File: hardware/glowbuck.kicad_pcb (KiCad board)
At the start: 4 copper layers, 80 x 50 mm, 128 parts, among them J1 Conn_01x04_Socket, J101 Conn_01x01_Pin, J102 Conn_01x01_Pin, J105 Conn_01x01_Pin, J106 Conn_01x01_Pin, J107 Conn_01x01_Pin, J201 USB_C_Receptacle_USB2.0_16P, J202 USB_C_Receptacle_USB2.0_16P, J3 Conn_02x08_Counter_Clockwise, Q401 2N7002NXAKR, SW101 SW_Push, SW102 SW_Push, U101 ESP32-S3-WROOM-1, U102 SN74LVC1T45DBV, U103 INA181A3, U201 TPS25730D, U202 TPD2E2U06DCK, U301 AP63203WU, U401 SIC437A

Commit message: Global labels, explanation texts, fix spring connector
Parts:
- removed J101, J102: Conn_01x01_Pin, TestPoint:TestPoint_Pad_3.0x3.0mm
- added H4: MountingHole, MountingHole:MountingHole_2.2mm_M2_DIN965_Pad_TopBottom, F.Cu at (106.0, 87.0)
- added TP106: TestPoint, TestPoint:TestPoint_Pad_3.0x3.0mm, F.Cu at (-6.50, 106.0)
- added TP107: TestPoint, TestPoint:TestPoint_Pad_3.0x3.0mm, F.Cu at (-6.50, 111.0)
- moved J202 350.7 mm to (116.0, 53.7), turned to 180 degrees
- moved C3 340.8 mm to (21.2, 192.8)
- moved C401 340.8 mm to (42.9, 196.5)
- moved C402 340.8 mm to (21.2, 195.3)
- moved C406 340.8 mm to (21.2, 197.8)
- moved C407 340.8 mm to (21.2, 200.4)
- moved C408 340.8 mm to (21.2, 202.9)
- moved C409 340.8 mm to (21.2, 205.4)
- moved L401 340.8 mm to (30.0, 182.2)
- moved R402 340.8 mm to (25.2, 192.8)
- moved R403 340.8 mm to (25.2, 195.3)
- moved R404 340.8 mm to (25.2, 197.8)
- moved R405 340.8 mm to (25.2, 200.4)
- moved R406 340.8 mm to (25.2, 202.9)
- moved R407 340.8 mm to (25.2, 205.4)
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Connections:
- net /BUCK_DISABLE renamed BUCK_DISABLE
- net /CURSENSE_V renamed CURSENSE_V
- net /LED_D0_3V3 renamed LED_D0_3V3
- net /LIGHT_SENSE renamed LIGHT_SENSE
- net /SCK renamed SCK
- net /SDA renamed SDA
- net /USB_N renamed USB_N
- net /USB_P renamed USB_P
- net Net-(D103-A) renamed /AUX_LED_GREEN
- net VCC renamed VBUS
- J3 pad 7: /GPIO5 -> GPIO4
- J3 pad 8: /GPIO4 -> GPIO5
- U101 pad 4: /GPIO4 -> GPIO4
- U101 pad 5: /GPIO5 -> GPIO5
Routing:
- added copper zone on B.Cu, net GND
- added copper zone on F.Cu, net GND
- added copper zone on In1.Cu, net GND
- added copper zone on In2.Cu, net GND
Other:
- outline, holes or cut-outs redrawn

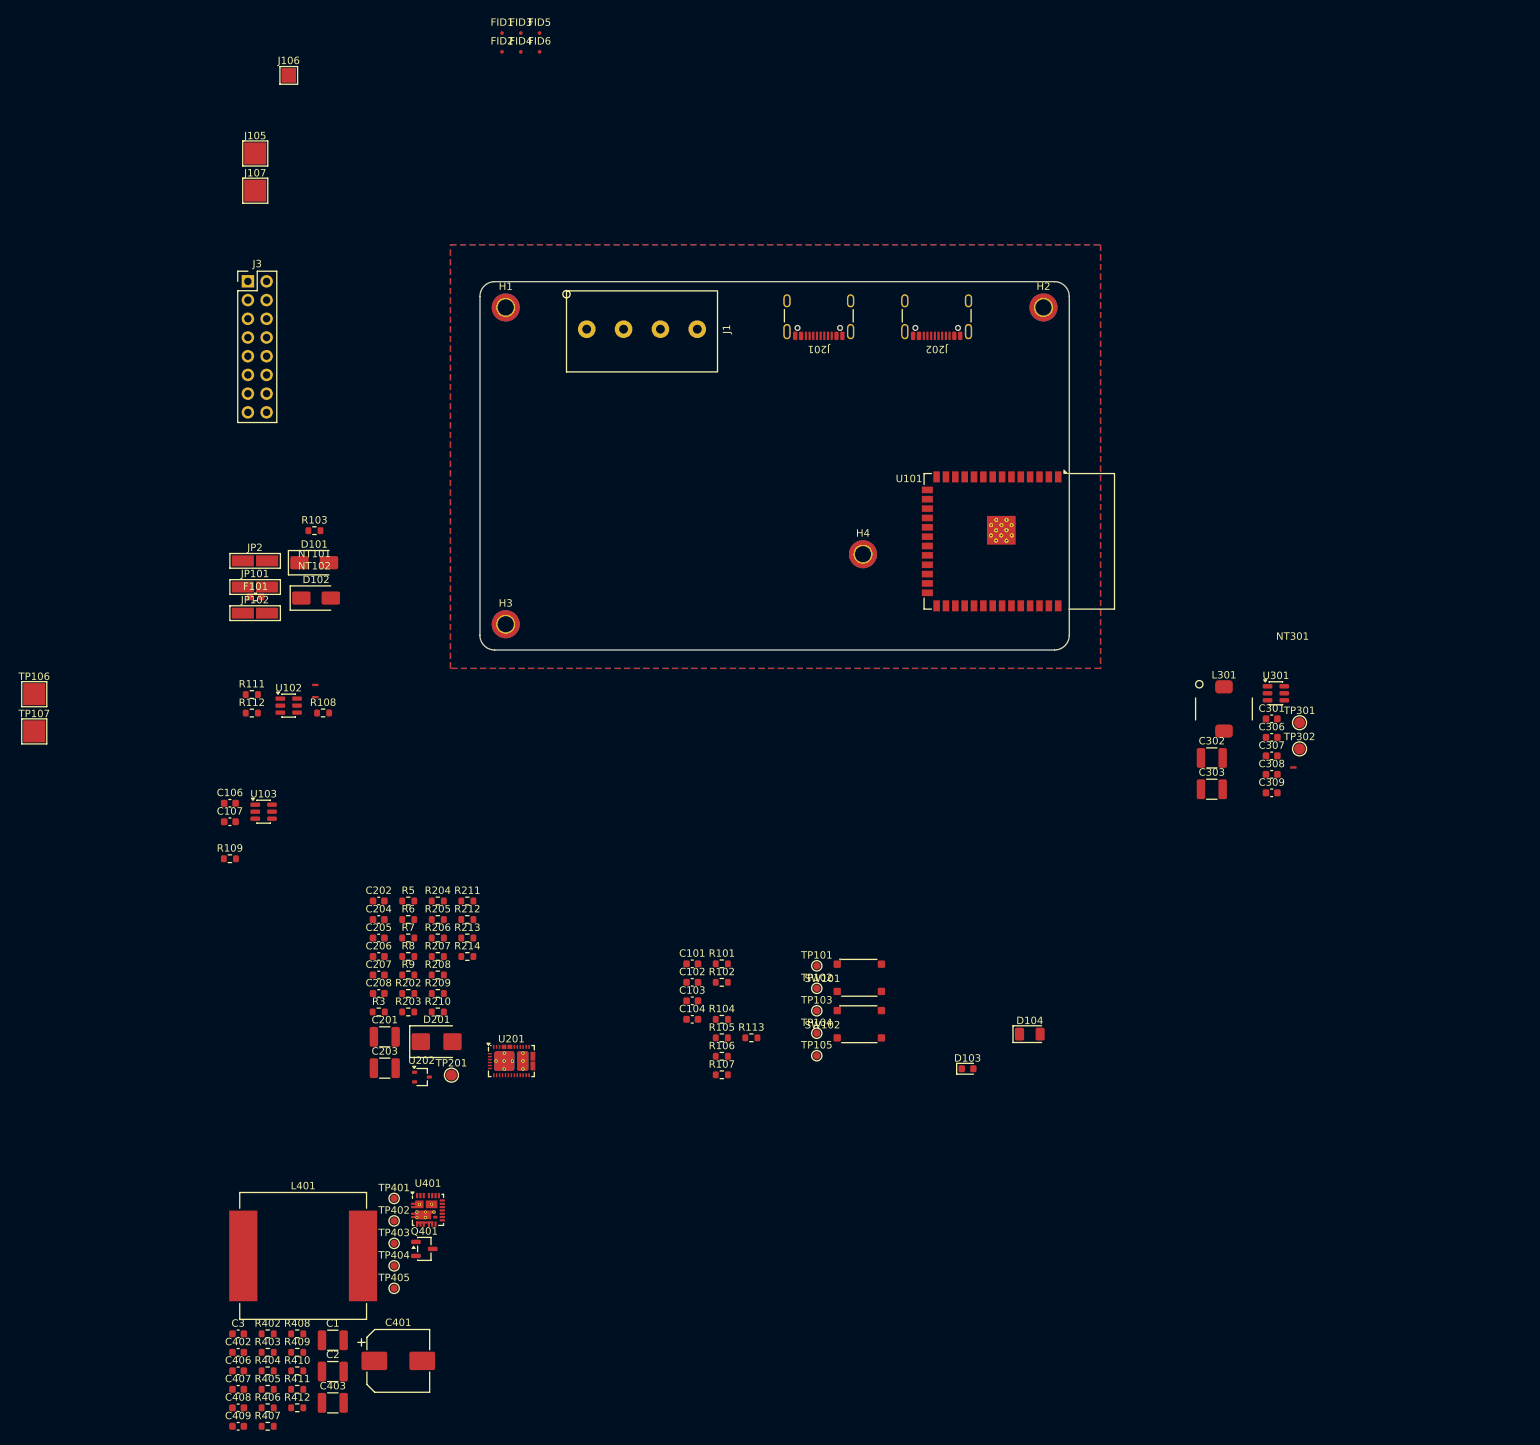
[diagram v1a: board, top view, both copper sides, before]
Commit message: Layout Stecker final, USB done, buck wip
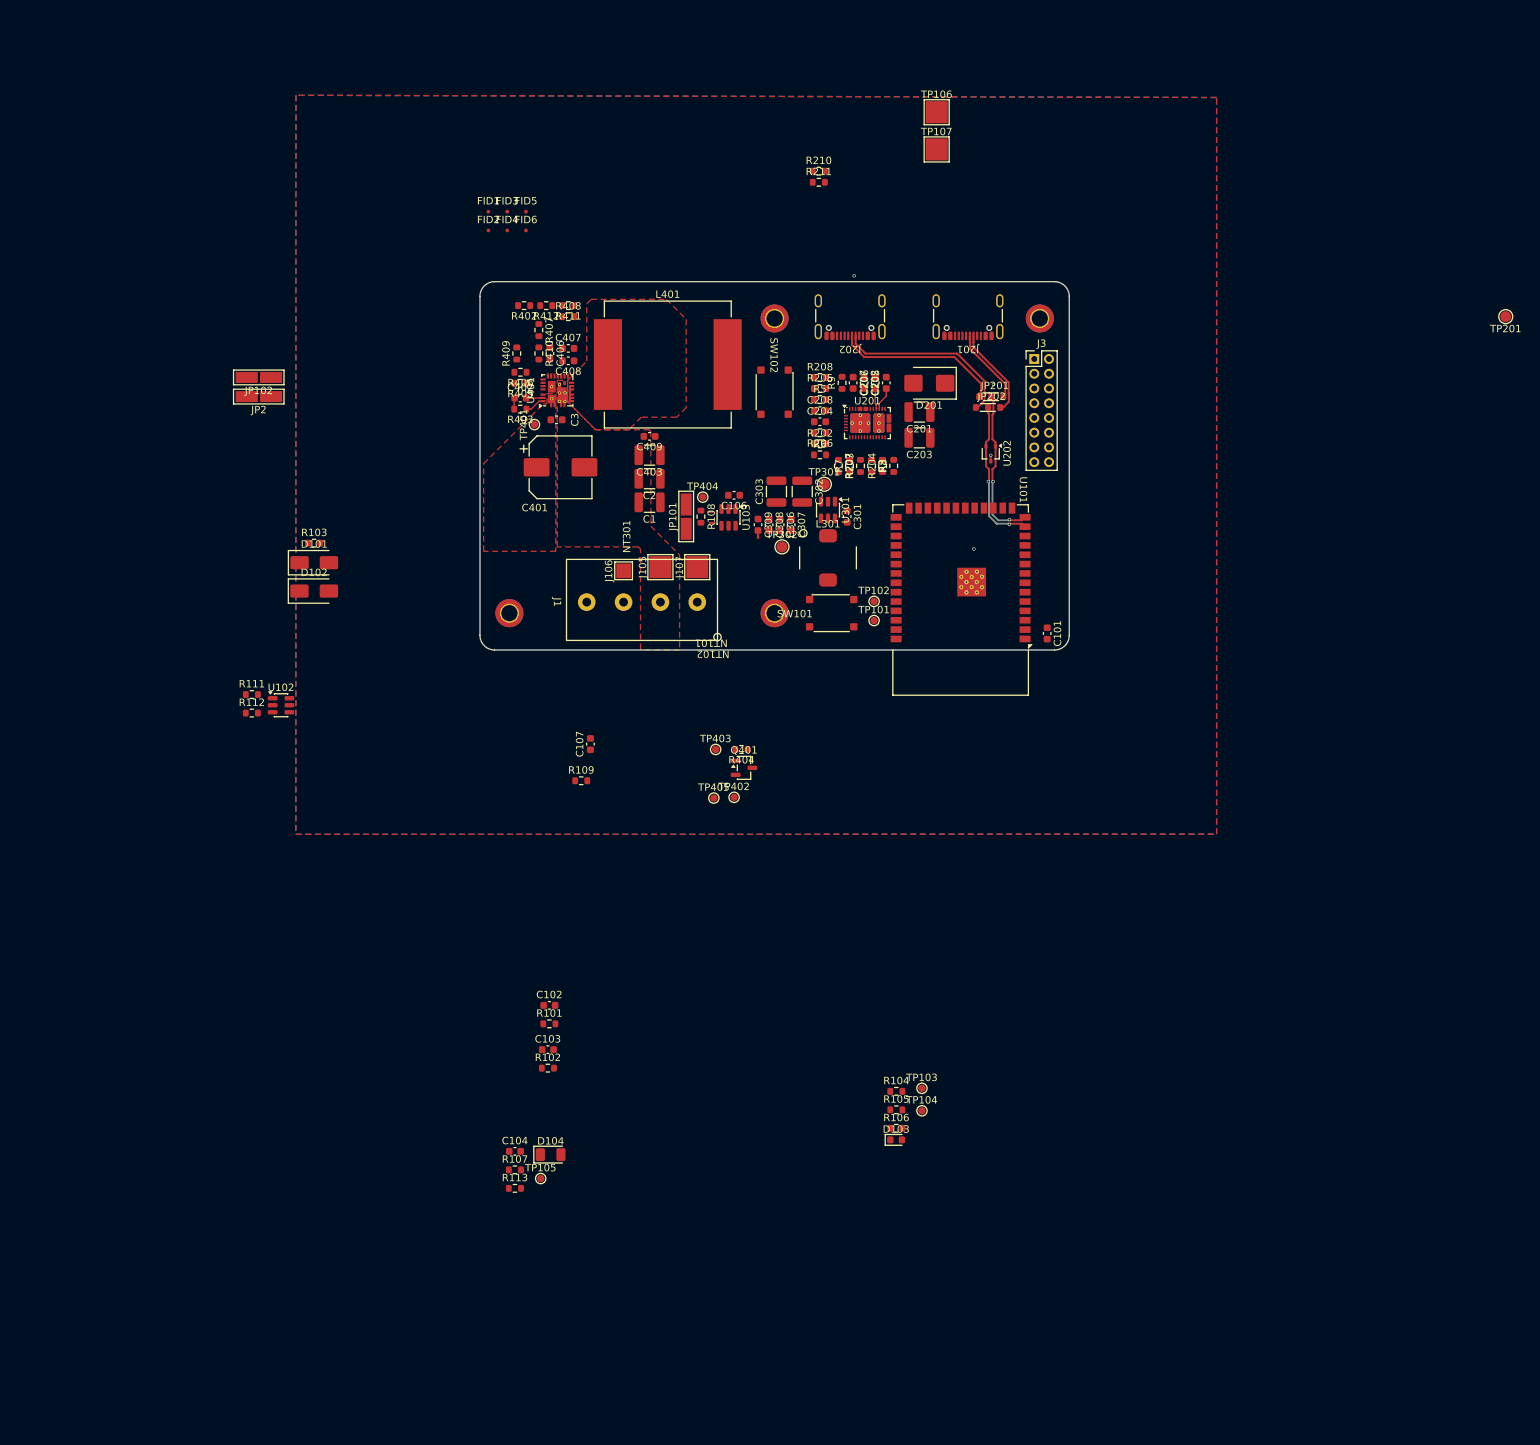
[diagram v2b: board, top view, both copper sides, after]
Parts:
- removed F101: FCC16252ADTP, Fuse:Fuse_0603_1608Metric
- removed R209, R212, R213, R214: 0R, Resistor_SMD:R_0603_1608Metric
- added JP201: SolderJumper_3_Bridged12, glowbuck:SolderJumper_123_0603, F.Cu at (123.4, 65.6)
- added JP202: SolderJumper_3_Bridged12, glowbuck:SolderJumper_123_0603, F.Cu at (123.0, 67.1)
- J3: footprint Connector_PinHeader_2.54mm:PinHeader_2x08_P2.54mm_Vertical -> Connector_PinHeader_2.00mm:PinHeader_2x08_P2.00mm_Vertical
- moved TP201 176.3 mm to (193.2, 54.8), turned to 180 degrees
- moved R412 153.4 mm to (63.0, 53.2), turned to 180 degrees
- moved R407 153.3 mm to (62.0, 56.6), turned to -90 degrees
- moved R411 151.6 mm to (66.0, 53.2), turned to 180 degrees
- moved C408 149.0 mm to (66.0, 60.8), turned to 180 degrees
- moved C407 148.2 mm to (66.0, 59.1)
- moved TP106 145.8 mm to (116.0, 27.0)
- moved TP107 145.8 mm to (116.0, 32.0)
- moved C409 145.5 mm to (77.0, 71.0), turned to 180 degrees
- moved R406 144.7 mm to (59.5, 62.3), turned to 180 degrees
- moved C406 144.4 mm to (63.5, 59.8), turned to -90 degrees
- moved R402 143.9 mm to (60.0, 53.2), turned to 180 degrees
- moved R408 142.9 mm to (66.0, 54.8)
- moved R410 141.9 mm to (62.0, 59.8), turned to -90 degrees
- moved R405 140.8 mm to (59.5, 63.8), turned to 180 degrees
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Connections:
- R410 pad 2: GND -> GND1
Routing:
- net /USB-C and PD/USB_ESP_N: track 0.00 -> 24.9 mm
- net /USB-C and PD/USB_ESP_P: track 0.00 -> 22.8 mm
- net USB_P: track 0.00 -> 21.6 mm, vias 0 -> 2
- net USB_N: track 0.00 -> 20.8 mm, vias 0 -> 2
- net /USB-C and PD/USB_PD_N: track 0.00 -> 12.4 mm
- net /USB-C and PD/USB_PD_P: track 0.00 -> 10.4 mm
- net /USB-C and PD/USB_CC1: track 0.00 -> 3.16 mm
- net /USB-C and PD/USB_CC2: track 0.00 -> 2.82 mm
- net /Buck Power/PHASE: track 0.00 -> 2.71 mm
- net /Buck Power/BOOT: track 0.00 -> 2.32 mm
- net Net-(C402-Pad1): track 0.00 -> 1.52 mm
- net GND: track 0.00 -> 0.75 mm, vias 0 -> 3
- net (no net): vias 0 -> 1
- added copper zone on F.Cu, net /Buck Power/SW
- added copper zone on F.Cu, net VBUS
